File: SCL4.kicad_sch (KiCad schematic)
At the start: 38 parts, among them J1 spare1, J2 spare2, J3 Siemens_A1010-A263, J4 SP1, J5 SP2, J6 Conn_01x08, J7 5V out, U1 MC3487DX, U2 MC3487DX, U3 TRAM Size 2, U4 MC10H125 (20PLCC), U5 MC10H124 (20PLCC)

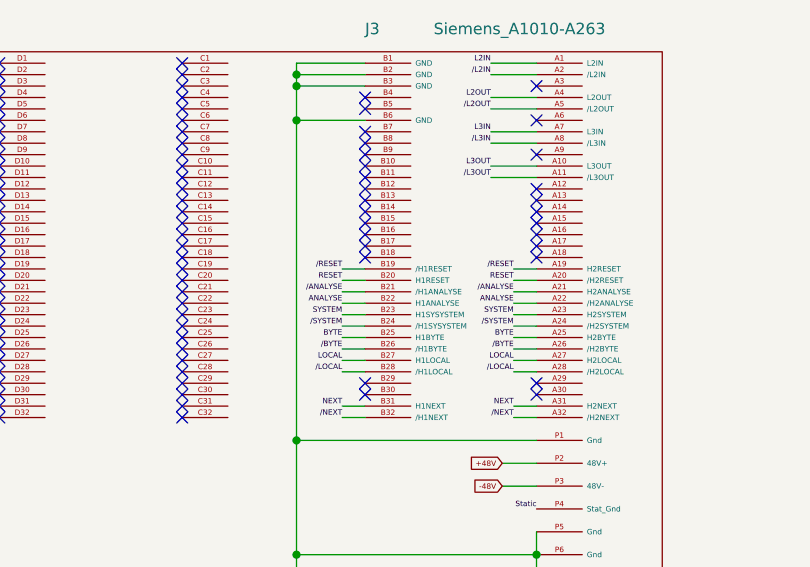
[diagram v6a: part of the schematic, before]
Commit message: correct differential orientation
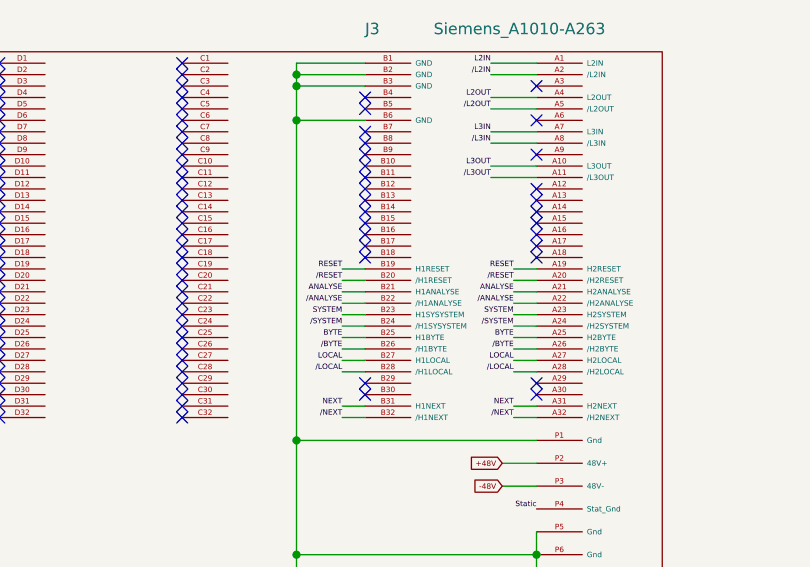
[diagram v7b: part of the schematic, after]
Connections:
- net ANALYSE: now also J3.A21 (H2ANALYSE), J3.B21 (H1ANALYSE); no longer J3.A22 (/H2ANALYSE), J3.B22 (H1ANALYSE)
- net RESET: now also J3.A19 (H2RESET), J3.B19 (H1RESET); no longer J3.A20 (/H2RESET), J3.B20 (H1RESET)
- net /ANALYSE: now also J3.A22 (/H2ANALYSE), J3.B22 (/H1ANALYSE); no longer J3.A21 (H2ANALYSE), J3.B21 (/H1ANALYSE)
- net /RESET: now also J3.A20 (/H2RESET), J3.B20 (/H1RESET); no longer J3.A19 (H2RESET), J3.B19 (/H1RESET)
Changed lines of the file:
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@@
     (effects (font (size 0.6 0.6)) (justify left bottom))
   )
-  (label "ANALYSE" (at 72.39 54.61 180)
+  (label "{slash}ANALYSE" (at 72.39 54.61 180)
     (effects (font (size 0.6 0.6)) (justify right bottom))
   )
@@
     (effects (font (size 1.27 1.27)) (justify right bottom))
   )
-  (label "ANALYSE" (at 91.44 54.61 180)
+  (label "{slash}ANALYSE" (at 91.44 54.61 180)
     (effects (font (size 0.6 0.6)) (justify right bottom))
   )
@@
     (effects (font (size 1.27 1.27)) (justify left bottom))
   )
-  (label "{slash}RESET" (at 91.44 50.8 180)
+  (label "RESET" (at 91.44 50.8 180)
     (effects (font (size 0.6 0.6)) (justify right bottom))
   )
@@
     (effects (font (size 1.27 1.27)) (justify left bottom))
   )
-  (label "RESET" (at 72.39 52.07 180)
+  (label "{slash}RESET" (at 72.39 52.07 180)
     (effects (font (size 0.6 0.6)) (justify right bottom))
   )
@@
     (effects (font (size 0.6 0.6)) (justify right bottom))
   )
-  (label "{slash}ANALYSE" (at 91.44 53.34 180)
+  (label "ANALYSE" (at 91.44 53.34 180)
     (effects (font (size 0.6 0.6)) (justify right bottom))
   )
@@
     (effects (font (size 0.6 0.6)) (justify left bottom))
   )
-  (label "{slash}ANALYSE" (at 72.39 53.34 180)
+  (label "ANALYSE" (at 72.39 53.34 180)
     (effects (font (size 0.6 0.6)) (justify right bottom))
   )
@@
     (effects (font (size 1.27 1.27)) (justify left bottom))
   )
-  (label "{slash}RESET" (at 72.39 50.8 180)
+  (label "RESET" (at 72.39 50.8 180)
     (effects (font (size 0.6 0.6)) (justify right bottom))
   )
@@
     (effects (font (size 0.6 0.6)) (justify right bottom))
   )
-  (label "RESET" (at 91.44 52.07 180)
-    (effects (font (size 0.6 0.6)) (justify right bottom))
-  )
+  (label "{slash}RESET" (at 91.44 52.07 180)
+    (effects (font (size 0.6 0.6)) (justify right bottom))
+  )
